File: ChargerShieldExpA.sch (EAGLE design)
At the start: 60 parts, among them IC1 LM324N, IC2 TL431, Q1 BD648, Q2 BUZ11, Q3 BUZ171, T2 BC548, X1 +5V, X2 Battery, X3 VCC

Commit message: reusable front panel
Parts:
- added LED5, LED6: (no value), bigger:LED5MM_BIG
- added R26, R27: 470, rcl:R-EU_0207/12
- added S5: A, bigger:SWITCH-MOMENTARY-2PTH_UMSE
- added S6: B, bigger:SWITCH-MOMENTARY-2PTH_UMSE
- S1, S2, S3, S4: device SparkFun-Electromechanical:SWITCH-MOMENTARY-2PTH -> bigger:SWITCH-MOMENTARY-2PTH_UMSE
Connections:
- new net N$37: S5.2, U$3.6
- new net N$38: S6.2, U$3.7
- new net N$39: LED5.A, R26.2
- new net N$40: LED6.A, R27.2
- new net N$41: R26.1, U$6.6
- new net N$42: R27.1, U$6.7
- net GND2: now also LED5.C, LED6.C, S5.1, S6.1
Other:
- moved on the sheet: LED1, LED2, LED3, LED4, R1, R20, R23, R3

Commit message: front board interconnections
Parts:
- added JP5: (no value), bigger:JP2E
- R26, R27: device rcl:R-EU_0207/12 -> rcl:R-EU_0204/7
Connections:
- removed net N$22: S3.2, U$3.4
- removed net N$3: S1.2, U$3.2
- removed net N$32: S4.2, U$3.5
- removed net N$33: R3.2, U$6.3
- removed net N$34: R1.2, U$6.2
- removed net N$35: R20.1, U$6.4
- removed net N$36: R23.1, U$6.5
- net +5V: now also JP5.3; no longer C4.1, IC1P.V+
- net N$1: now also R1.2, U$6.2
- net N$19: now also R3.2, U$6.3
- net N$23: now also S4.2, U$3.5
- net N$26: now also S1.2, U$3.2
- net N$30: now also S2.2, U$3.3
- net N$31: now also S3.2, U$3.4
- net N$37: now also U$4.6
- net N$38: now also U$4.7
- net N$4: now also C4.1, IC1P.V+, JP5.2; no longer S2.2, U$3.3
- net N$41: now also U$5.6
- net N$42: now also U$5.7
- net PWM_DISCHARGE1: now also R20.1, U$6.4
- net PWM_DISCHARGE2: now also R23.1, U$6.5
- net VCC: now also JP5.1

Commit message: opamp test circuitry
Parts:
- added JP10, JP11, JP12, JP13, JP14, JP4, JP6, JP7, JP8: (no value), bigger:JP1E
- added JP9: (no value), bigger:JP2E
- added R28, R29, R30, R31, R32, R34: 0, rcl:R-EU_0204/7
- added R33: 0, rcl:R-EU_0204/2V
- R24: value 1k -> 0
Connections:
- new net N$22: JP6.1, R14.2
- new net N$3: C1.+, JP4.1, R13.2, R8.2
- new net N$32: JP7.1, R12.2
- new net N$33: JP8.2, R24.2
- new net N$34: IC1C.OUT, JP11.1, R33.1
- new net N$36: IC1D.-IN, R29.1, R31.1
- new net N$43: IC1C.+IN, JP10.2
- new net N$44: JP10.1, R28.1
- new net N$45: IC1D.+IN, R30.1, R32.2
- new net N$46: JP12.1, JP12.2, R30.2
- new net N$47: JP13.1, JP13.2, R31.2
- new net N$48: IC1D.OUT, JP14.1, JP14.2, R32.1
- new net N$49: IC1C.-IN, R33.2, R34.1
- net +5V: now also JP9.1
- net GND: now also JP9.3, R28.2, R29.2, R34.2
- net I_SENSE: now also JP6.2; no longer R14.2
- net N$11: now also JP7.2; no longer R12.2
- net N$25: now also JP8.1; no longer R24.2
- net U_BATT1: now also JP4.2; no longer C1.+, R13.2, R8.2
- net VCC: now also JP9.2

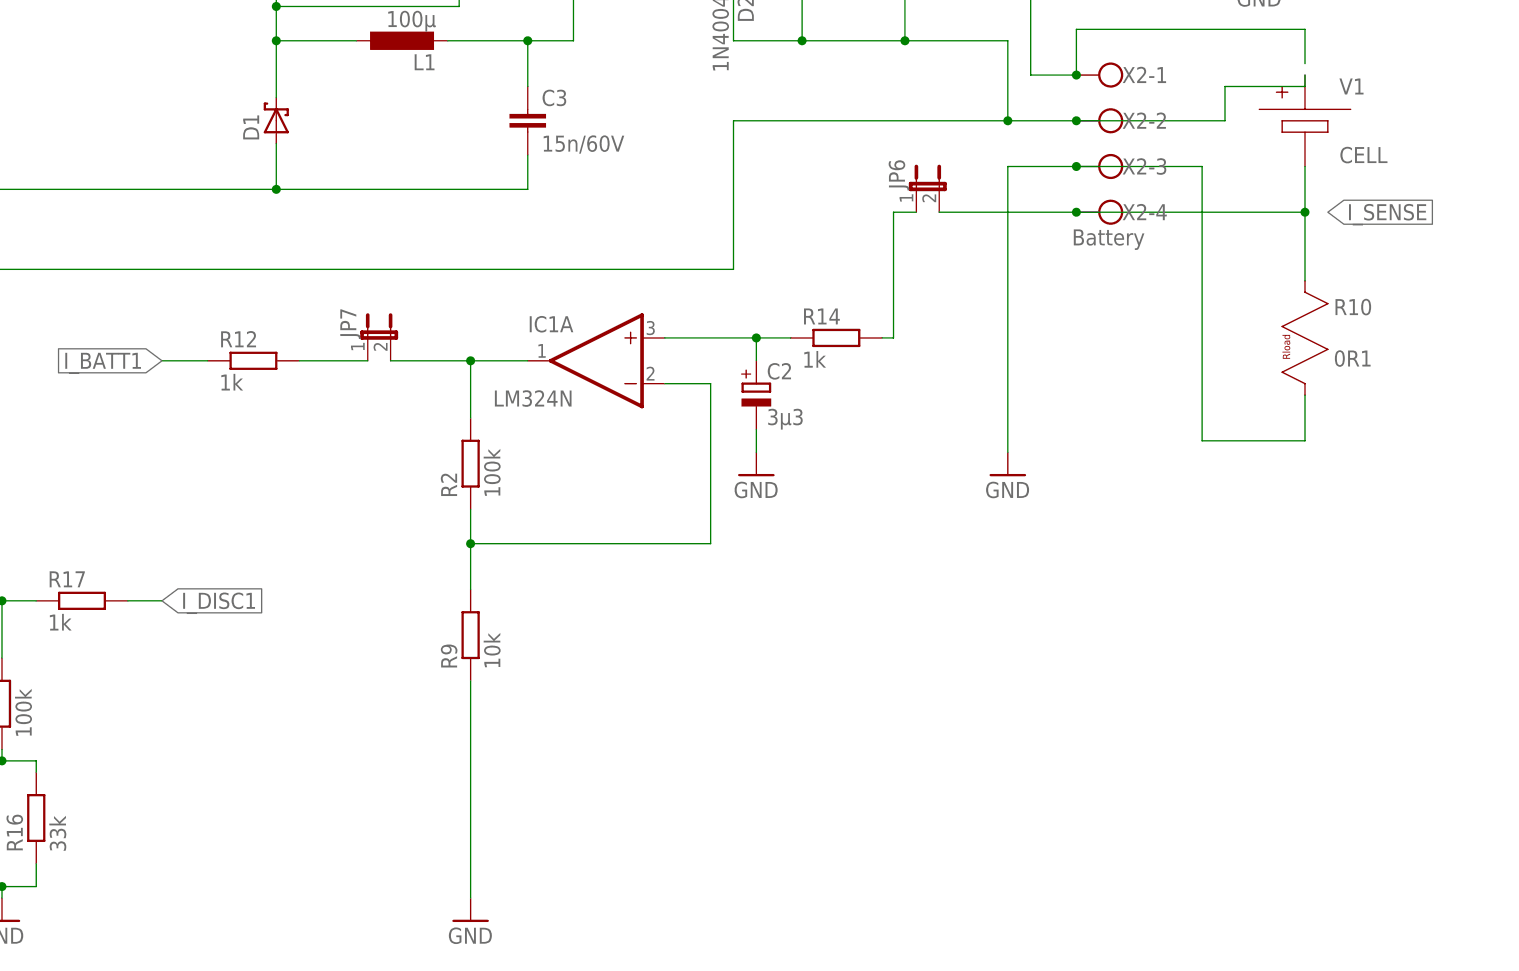
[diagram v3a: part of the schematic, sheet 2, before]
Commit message: difference amplifier at charge current
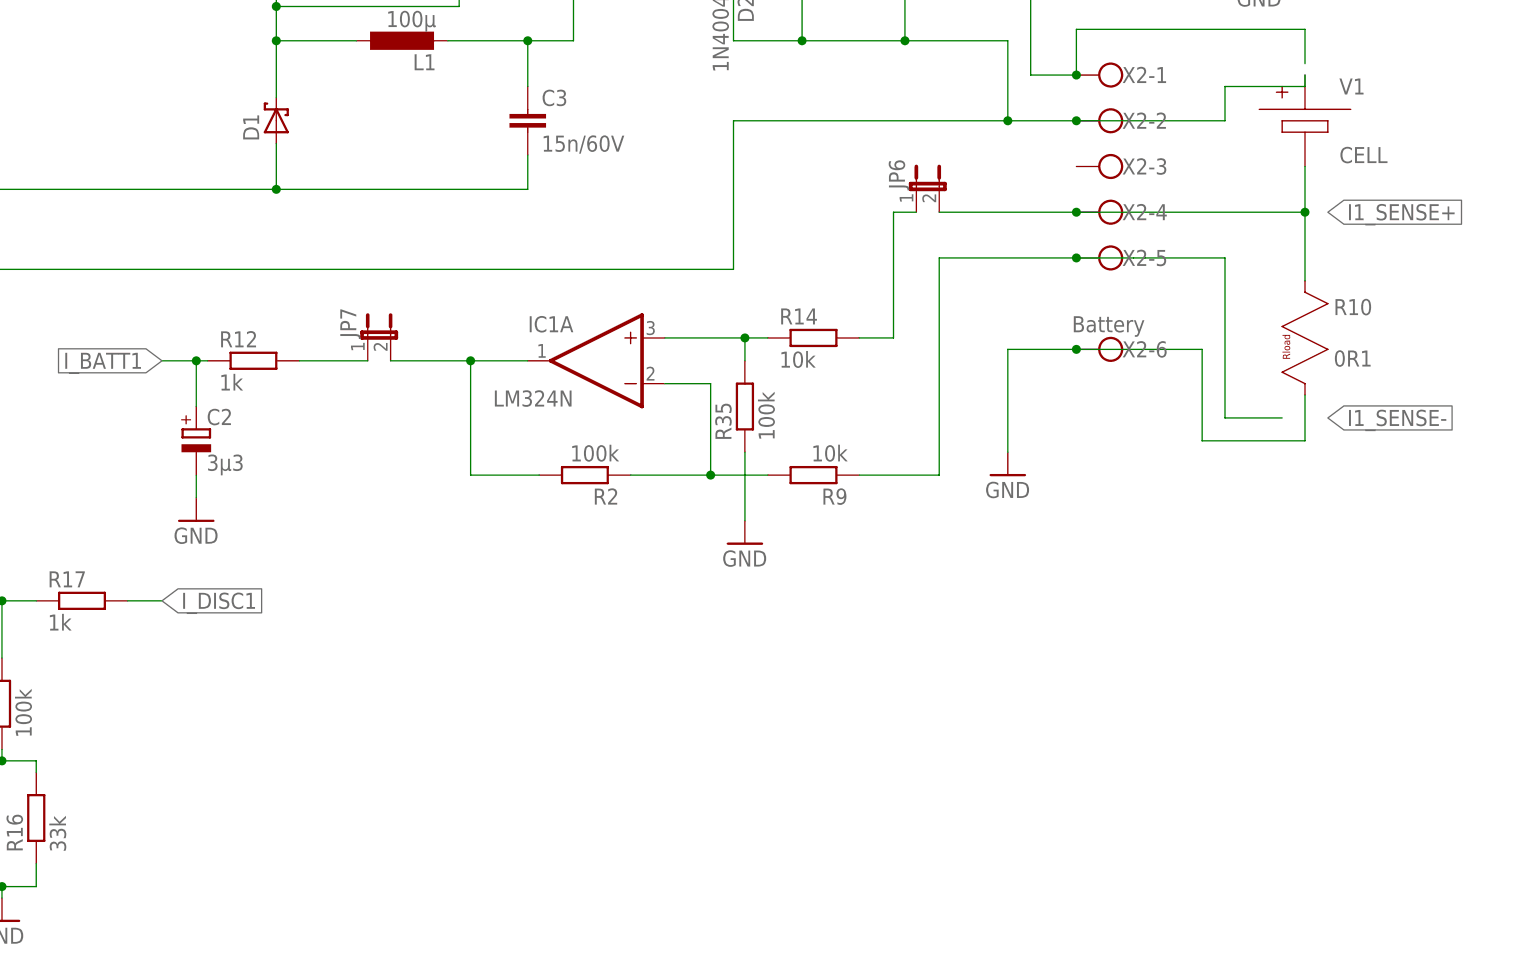
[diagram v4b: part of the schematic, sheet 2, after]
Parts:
- added R35: 100k, rcl:R-EU_0204/7
- R14: value 1k -> 10k
- R9: device rcl:R-EU_0204/7 -> rcl:R-EU_0207/12
- X2: device con-wago-500:W237-4 -> con-wago-500:W237-6
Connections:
- net I_SENSE renamed I1_SENSE+
- new net I1_SENSE-: R9.1, X2-5.KL
- net GND: now also R35.1, X2-6.KL; no longer R9.1, X2-3.KL
- net I_BATT1: now also C2.+
- net N$15: now also R35.2; no longer C2.+
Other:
- moved on the sheet: C2, R14, R2, R9
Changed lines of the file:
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@@
 <part name="U$1" library="arduino-long" deviceset="ARDUINOR3" device="BPLACE-LONG" value="ARDUINOR3BPLACE-LONG"/>
 <part name="X1" library="con-wago-500" deviceset="W237-102" device="" value="+5V"/>
-<part name="X2" library="con-wago-500" deviceset="W237-4" device="" value="Battery"/>
+<part name="X2" library="con-wago-500" deviceset="W237-6" device="" value="Battery"/>
 <part name="LED1" library="bigger" deviceset="LED" device="5MM_BIG" value="CHRG1"/>
 <part name="S1" library="bigger" deviceset="SWITCH-MOMENTARY-2" device="PTH_UMSE" value="Down"/>
@@
 <part name="IC1" library="linear" deviceset="LM324" device="N"/>
 <part name="R2" library="rcl" deviceset="R-EU_" device="0204/7" value="100k"/>
-<part name="R9" library="rcl" deviceset="R-EU_" device="0204/7" value="10k"/>
-<part name="GND9" library="supply1" deviceset="GND" device=""/>
+<part name="R9" library="rcl" deviceset="R-EU_" device="0207/12" value="10k"/>
 <part name="R10" library="lt-spice-simulation" deviceset="RES_RLOAD" device="" value="0R1"/>
 <part name="R7" library="rcl" deviceset="R-EU_" device="0414/15" value="1R666"/>
@@
 <part name="R13" library="rcl" deviceset="R-EU_" device="0207/10" value="100k"/>
 <part name="C1" library="rcl" deviceset="CPOL-EU" device="E5-5" value="10µ"/>
-<part name="R14" library="rcl" deviceset="R-EU_" device="0207/10" value="1k"/>
+<part name="R14" library="rcl" deviceset="R-EU_" device="0207/10" value="10k"/>
 <part name="C2" library="rcl" deviceset="CPOL-EU" device="E5-5" value="3µ3"/>
 <part name="R15" library="rcl" deviceset="R-EU_" device="0207/10" value="100k"/>
@@
 <part name="R34" library="rcl" deviceset="R-EU_" device="0204/7" value="0"/>
 <part name="GND16" library="supply1" deviceset="GND" device=""/>
+<part name="R35" library="rcl" deviceset="R-EU_" device="0204/7" value="100k"/>
+<part name="GND9" library="supply1" deviceset="GND" device=""/>
 </parts>
 <sheets>
@@
 <instance part="L1" gate="G$1" x="143.51" y="116.84" rot="R90"/>
 <instance part="V1" gate="G$1" x="243.84" y="113.03"/>
-<instance part="GND5" gate="1" x="182.88" y="68.58"/>
+<instance part="GND5" gate="1" x="120.65" y="63.5"/>
 <instance part="D2" gate="1" x="180.34" y="124.46" rot="R270"/>
 <instance part="JP1" gate="A" x="191.77" y="125.73" rot="R270"/>
@@
 <instance part="P+4" gate="VCC" x="74.93" y="158.75"/>
 <instance part="IC1" gate="A" x="165.1" y="81.28" rot="MR0"/>
-<instance part="R2" gate="G$1" x="151.13" y="69.85" rot="R90"/>
-<instance part="R9" gate="G$1" x="151.13" y="50.8" rot="R90"/>
-<instance part="GND9" gate="1" x="151.13" y="19.05"/>
+<instance part="R2" gate="G$1" x="163.83" y="68.58" rot="R180"/>
+<instance part="R9" gate="G$1" x="189.23" y="68.58" rot="R180"/>
 <instance part="R10" gate="G$1" x="241.3" y="92.71"/>
 <instance part="R7" gate="G$1" x="52.07" y="40.64" rot="MR270"/>
@@
 <instance part="R13" gate="G$1" x="238.76" y="133.35" rot="R90"/>
 <instance part="C1" gate="G$1" x="228.6" y="134.62"/>
-<instance part="R14" gate="G$1" x="191.77" y="83.82"/>
-<instance part="C2" gate="G$1" x="182.88" y="78.74"/>
+<instance part="R14" gate="G$1" x="189.23" y="83.82"/>
+<instance part="C2" gate="G$1" x="120.65" y="73.66"/>
 <instance part="IC1" gate="B" x="86.36" y="54.61"/>
 <instance part="R15" gate="G$1" x="99.06" y="43.18" rot="R90"/>
@@
 <instance part="JP7" gate="A" x="139.7" y="83.82"/>
 <instance part="JP8" gate="A" x="55.88" y="59.69"/>
+<instance part="X2" gate="-5" x="223.52" y="92.71" rot="R180"/>
+<instance part="X2" gate="-6" x="223.52" y="82.55" rot="R180"/>
+<instance part="R35" gate="G$1" x="181.61" y="76.2" rot="R90"/>
+<instance part="GND9" gate="1" x="181.61" y="60.96"/>
 </instances>
 <busses>
@@
 <segment>
 <pinref part="GND7" gate="1" pin="GND"/>
-<wire x1="210.82" y1="102.87" x2="210.82" y2="71.12" width="0.1524" layer="91"/>
-<pinref part="X2" gate="-3" pin="KL"/>
-<wire x1="210.82" y1="102.87" x2="218.44" y2="102.87" width="0.1524" layer="91"/>
-<wire x1="218.44" y1="102.87" x2="232.41" y2="102.87" width="0.1524" layer="91"/>
-<junction x="218.44" y="102.87"/>
+<wire x1="210.82" y1="82.55" x2="210.82" y2="71.12" width="0.1524" layer="91"/>
 <wire x1="243.84" y1="77.47" x2="243.84" y2="72.39" width="0.1524" layer="91"/>
 <wire x1="243.84" y1="72.39" x2="232.41" y2="72.39" width="0.1524" layer="91"/>
-<wire x1="232.41" y1="72.39" x2="232.41" y2="102.87" width="0.1524" layer="91"/>
+<wire x1="232.41" y1="72.39" x2="232.41" y2="82.55" width="0.1524" layer="91"/>
 <pinref part="R10" gate="G$1" pin="B"/>
-</segment>
-<segment>
-<pinref part="R9" gate="G$1" pin="1"/>
-<pinref part="GND9" gate="1" pin="GND"/>
-<wire x1="151.13" y1="45.72" x2="151.13" y2="21.59" width="0.1524" layer="91"/>
+<pinref part="X2" gate="-6" pin="KL"/>
+<wire x1="210.82" y1="82.55" x2="218.44" y2="82.55" width="0.1524" layer="91"/>
+<wire x1="218.44" y1="82.55" x2="232.41" y2="82.55" width="0.1524" layer="91"/>
+<junction x="218.44" y="82.55"/>
 </segment>
 <segment>
 <pinref part="C2" gate="G$1" pin="-"/>
 <pinref part="GND5" gate="1" pin="GND"/>
-<wire x1="182.88" y1="73.66" x2="182.88" y2="71.12" width="0.1524" layer="91"/>
+<wire x1="120.65" y1="68.58" x2="120.65" y2="66.04" width="0.1524" layer="91"/>
 </segment>
 <segment>
@@
 <wire x1="72.39" y1="22.86" x2="58.42" y2="22.86" width="0.1524" layer="91"/>
 <junction x="58.42" y="22.86"/>
+</segment>
+<segment>
+<pinref part="R35" gate="G$1" pin="1"/>
+<pinref part="GND9" gate="1" pin="GND"/>
+<wire x1="181.61" y1="71.12" x2="181.61" y2="63.5" width="0.1524" layer="91"/>
 </segment>
 </net>
@@
 </segment>
 </net>
-<net name="I_SENSE" class="0">
+<net name="I1_SENSE+" class="0">
 <segment>
 <pinref part="V1" gate="G$1" pin="-"/>
@@
 <pinref part="R2" gate="G$1" pin="2"/>
 <wire x1="157.48" y1="81.28" x2="151.13" y2="81.28" width="0.1524" layer="91"/>
-<wire x1="151.13" y1="81.28" x2="151.13" y2="74.93" width="0.1524" layer="91"/>
+<wire x1="151.13" y1="81.28" x2="151.13" y2="68.58" width="0.1524" layer="91"/>
+<wire x1="151.13" y1="68.58" x2="158.75" y2="68.58" width="0.1524" layer="91"/>
 <wire x1="151.13" y1="81.28" x2="142.24" y2="81.28" width="0.1524" layer="91"/>
 <junction x="151.13" y="81.28"/>
@@
 <segment>
 <pinref part="R2" gate="G$1" pin="1"/>
-<wire x1="151.13" y1="64.77" x2="151.13" y2="60.96" width="0.1524" layer="91"/>
-<wire x1="151.13" y1="60.96" x2="177.8" y2="60.96" width="0.1524" layer="91"/>
-<wire x1="177.8" y1="60.96" x2="177.8" y2="78.74" width="0.1524" layer="91"/>
+<wire x1="168.91" y1="68.58" x2="177.8" y2="68.58" width="0.1524" layer="91"/>
+<wire x1="177.8" y1="68.58" x2="177.8" y2="78.74" width="0.1524" layer="91"/>
 <pinref part="IC1" gate="A" pin="-IN"/>
 <wire x1="177.8" y1="78.74" x2="172.72" y2="78.74" width="0.1524" layer="91"/>
 <pinref part="R9" gate="G$1" pin="2"/>
-<wire x1="151.13" y1="55.88" x2="151.13" y2="60.96" width="0.1524" layer="91"/>
-<junction x="151.13" y="60.96"/>
+<wire x1="184.15" y1="68.58" x2="177.8" y2="68.58" width="0.1524" layer="91"/>
+<junction x="177.8" y="68.58"/>
 </segment>
 </net>
@@
 <segment>
 <pinref part="IC1" gate="A" pin="+IN"/>
-<wire x1="172.72" y1="83.82" x2="182.88" y2="83.82" width="0.1524" layer="91"/>
+<wire x1="172.72" y1="83.82" x2="181.61" y2="83.82" width="0.1524" layer="91"/>
 <pinref part="R14" gate="G$1" pin="1"/>
+<pinref part="R35" gate="G$1" pin="2"/>
+<wire x1="181.61" y1="83.82" x2="184.15" y2="83.82" width="0.1524" layer="91"/>
+<wire x1="181.61" y1="83.82" x2="181.61" y2="81.28" width="0.1524" layer="91"/>
+<junction x="181.61" y="83.82"/>
+</segment>
+</net>
+<net name="I_BATT1" class="0">
+<segment>
+<pinref part="R12" gate="G$1" pin="1"/>
+<wire x1="121.92" y1="81.28" x2="120.65" y2="81.28" width="0.1524" layer="91"/>
+<label x="116.84" y="81.28" size="1.778" layer="95" rot="R180" xref="yes"/>
 <pinref part="C2" gate="G$1" pin="+"/>
-<wire x1="182.88" y1="83.82" x2="186.69" y2="83.82" width="0.1524" layer="91"/>
-<wire x1="182.88" y1="83.82" x2="182.88" y2="81.28" width="0.1524" layer="91"/>
-<junction x="182.88" y="83.82"/>
-</segment>
-</net>
-<net name="I_BATT1" class="0">
-<segment>
-<pinref part="R12" gate="G$1" pin="1"/>
-<wire x1="121.92" y1="81.28" x2="116.84" y2="81.28" width="0.1524" layer="91"/>
-<label x="116.84" y="81.28" size="1.778" layer="95" rot="R180" xref="yes"/>
+<wire x1="120.65" y1="81.28" x2="116.84" y2="81.28" width="0.1524" layer="91"/>
+<wire x1="120.65" y1="81.28" x2="120.65" y2="76.2" width="0.1524" layer="91"/>
+<junction x="120.65" y="81.28"/>
 </segment>
 </net>
@@
 <wire x1="200.66" y1="97.79" x2="198.12" y2="97.79" width="0.1524" layer="91"/>
 <wire x1="198.12" y1="97.79" x2="198.12" y2="83.82" width="0.1524" layer="91"/>
-<wire x1="198.12" y1="83.82" x2="196.85" y2="83.82" width="0.1524" layer="91"/>
+<wire x1="198.12" y1="83.82" x2="194.31" y2="83.82" width="0.1524" layer="91"/>
 </segment>
 </net>
@@
 </segment>
 </net>
+<net name="I1_SENSE-" class="0">
+<segment>
+<wire x1="234.95" y1="92.71" x2="226.06" y2="92.71" width="0.1524" layer="91"/>
+<wire x1="226.06" y1="92.71" x2="224.79" y2="92.71" width="0.1524" layer="91"/>
+<wire x1="234.95" y1="74.93" x2="234.95" y2="92.71" width="0.1524" layer="91"/>
+<wire x1="234.95" y1="74.93" x2="241.3" y2="74.93" width="0.1524" layer="91"/>
+<pinref part="X2" gate="-5" pin="KL"/>
+<wire x1="218.44" y1="92.71" x2="203.2" y2="92.71" width="0.1524" layer="91"/>
+<pinref part="R9" gate="G$1" pin="1"/>
+<wire x1="194.31" y1="68.58" x2="203.2" y2="68.58" width="0.1524" layer="91"/>
+<wire x1="203.2" y1="68.58" x2="203.2" y2="92.71" width="0.1524" layer="91"/>
+<wire x1="224.79" y1="92.71" x2="218.44" y2="92.71" width="0.1524" layer="91"/>
+<junction x="218.44" y="92.71"/>
+<label x="246.38" y="74.93" size="1.778" layer="95" xref="yes"/>
+</segment>
+</net>
